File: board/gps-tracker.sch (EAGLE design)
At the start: 30 parts, among them J2 AVR_SPI_PRG_6OFFSET_PADS, U2 MCP73831, U3 ATMEGA328P, X1 USBSMD

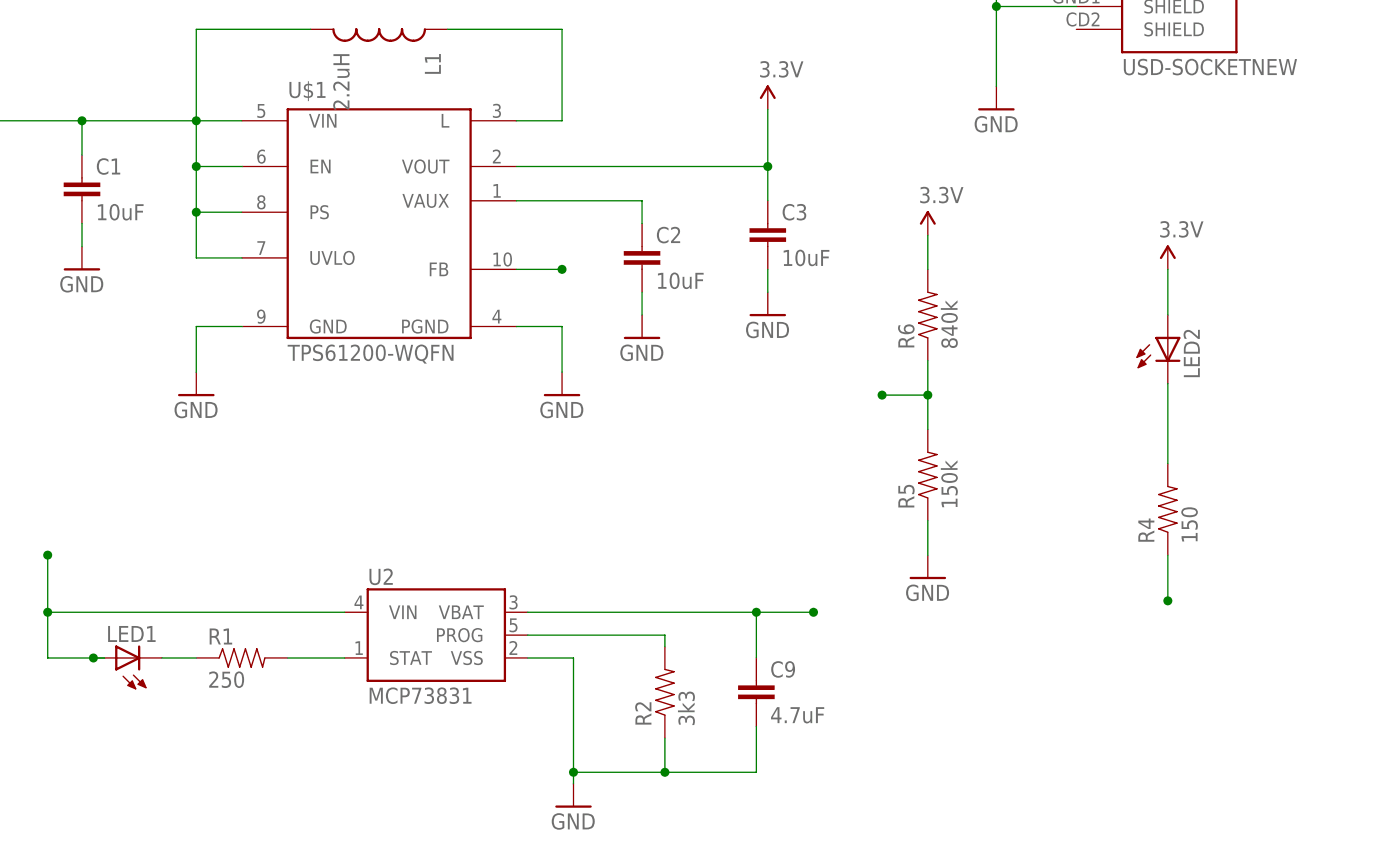
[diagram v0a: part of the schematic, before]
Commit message: Adding UVLO
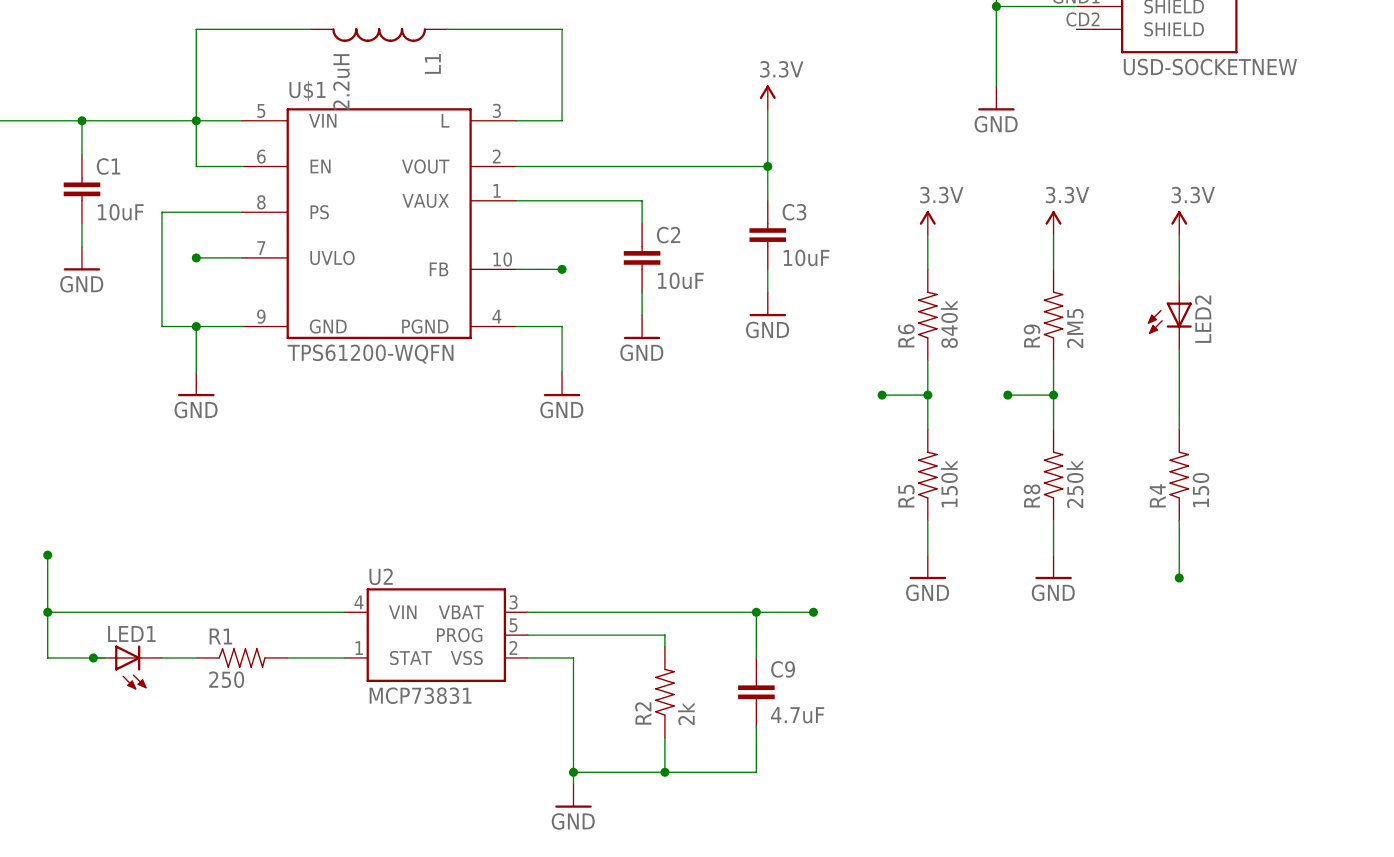
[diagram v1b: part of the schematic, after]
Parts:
- added R8: 250k, SparkFun:RESISTOR0603-RES
- added R9: 2M5, SparkFun:RESISTOR0603-RES
- R2: value 3k3 -> 2k
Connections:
- new net UVLO: R8.2, R9.1, U$1.UVLO
- net 3.3V: now also R9.2
- net GND: now also R8.1, U$1.PS
- net VBATT: no longer U$1.PS, U$1.UVLO
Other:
- moved on the sheet: LED2, R4
